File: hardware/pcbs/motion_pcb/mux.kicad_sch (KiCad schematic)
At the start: 2 parts, among them U3 74HC4051

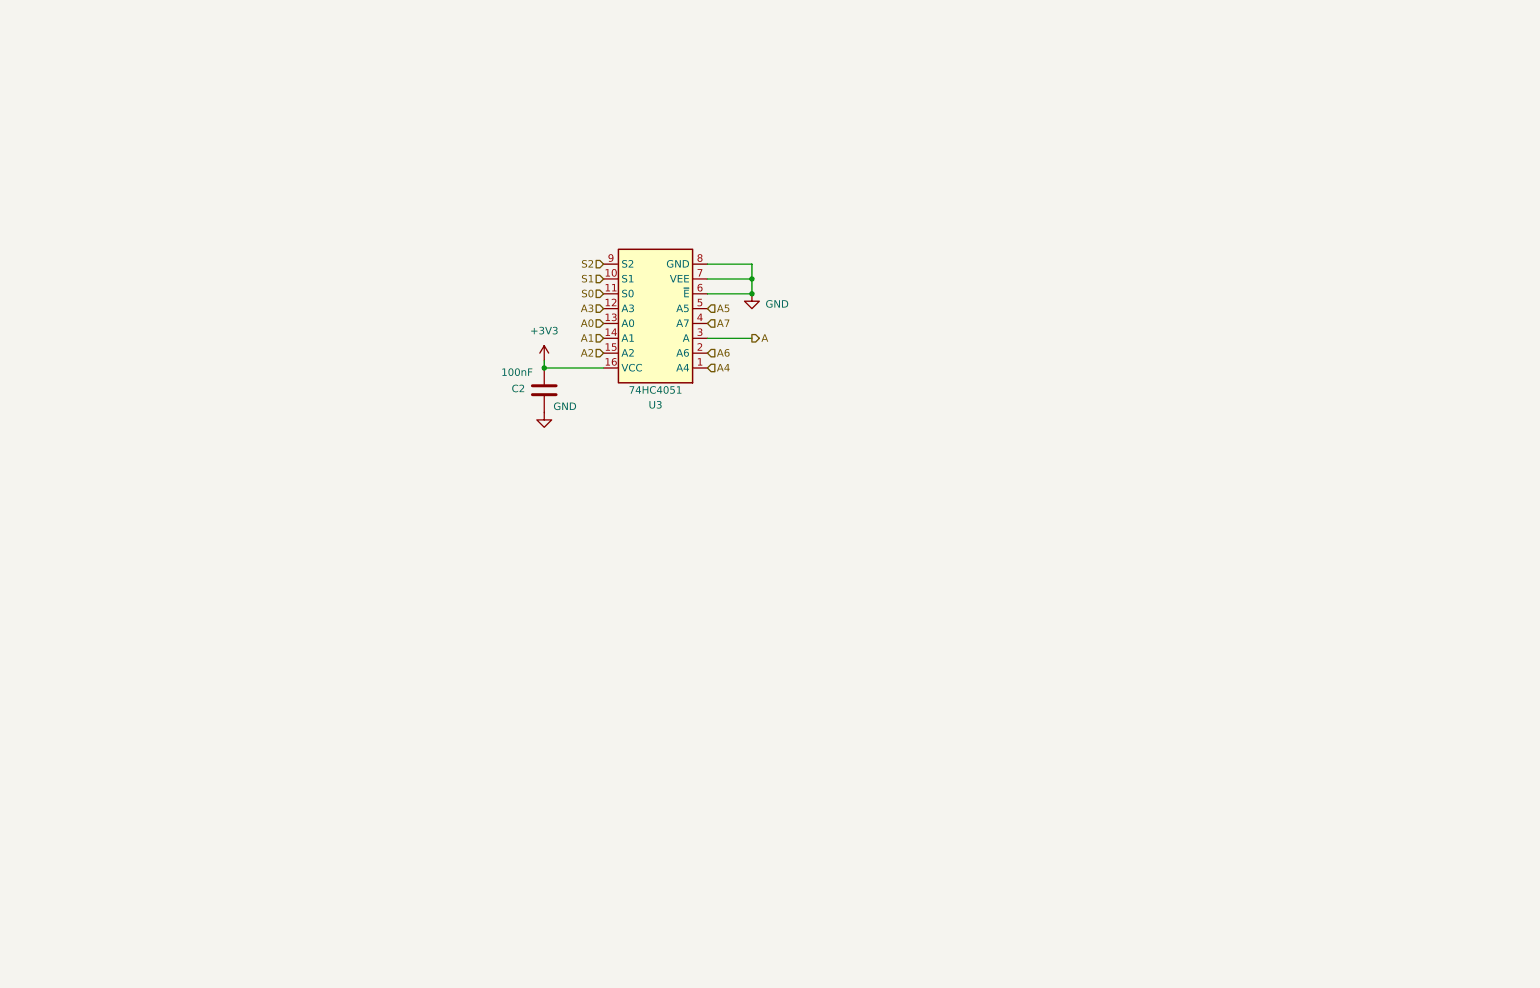
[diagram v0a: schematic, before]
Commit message: changing labels
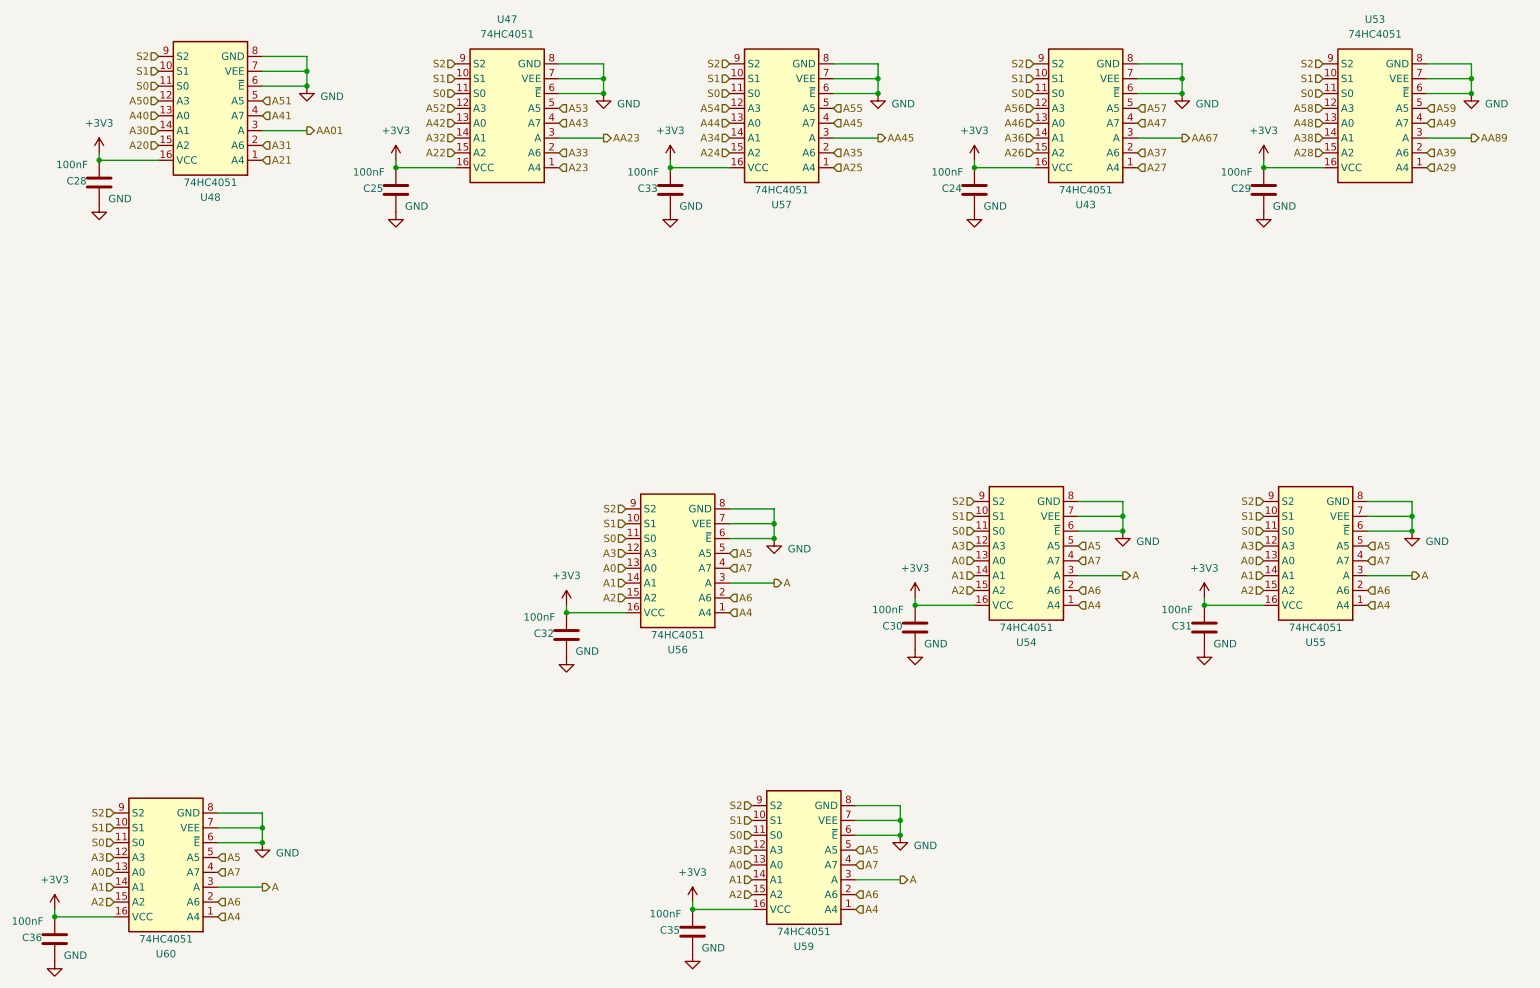
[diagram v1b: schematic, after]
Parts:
- added C24, C25, C28, C30, C31, C32, C33, C35, C36: 100nF, Capacitor_SMD:C_1206_3216Metric_Pad1.33x1.80mm_HandSolder, symbol Device:C
- added U43, U47, U48, U54, U55, U56, U57, U59, U60: 74HC4051, Package_SO:SOIC-16_3.9x9.9mm_P1.27mm, symbol 3dAudioSym:74HC4051
- U53: renamed from U3; footprint (none) -> Package_SO:SOIC-16_3.9x9.9mm_P1.27mm
- renumbered C2 to C29
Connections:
- net +3V3: now also C24.1, C25.1, C28.1, C30.1, C31.1, C32.1, C33.1, C35.1, C36.1, U43.16 (VCC), U47.16 (VCC), U48.16 (VCC), U54.16 (VCC), U55.16 (VCC), U56.16 (VCC), U57.16 (VCC), U59.16 (VCC), U60.16 (VCC)
- net A: now also U54.3 (A), U55.3 (A), U56.3 (A), U59.3 (A), U60.3 (A); no longer U53.3 (A)
- net A0: now also U54.13 (A0), U55.13 (A0), U56.13 (A0), U59.13 (A0), U60.13 (A0); no longer U53.13 (A0)
- net A1: now also U54.14 (A1), U55.14 (A1), U56.14 (A1), U59.14 (A1), U60.14 (A1); no longer U53.14 (A1)
- net A2: now also U54.15 (A2), U55.15 (A2), U56.15 (A2), U59.15 (A2), U60.15 (A2); no longer U53.15 (A2)
- net A3: now also U54.12 (A3), U55.12 (A3), U56.12 (A3), U59.12 (A3), U60.12 (A3); no longer U53.12 (A3)
- net A4: now also U54.1 (A4), U55.1 (A4), U56.1 (A4), U59.1 (A4), U60.1 (A4); no longer U53.1 (A4)
- net A5: now also U54.5 (A5), U55.5 (A5), U56.5 (A5), U59.5 (A5), U60.5 (A5); no longer U53.5 (A5)
- net A6: now also U54.2 (A6), U55.2 (A6), U56.2 (A6), U59.2 (A6), U60.2 (A6); no longer U53.2 (A6)
- net A7: now also U54.4 (A7), U55.4 (A7), U56.4 (A7), U59.4 (A7), U60.4 (A7); no longer U53.4 (A7)
- net GND: now also C24.2, C25.2, C28.2, C30.2, C31.2, C32.2, C33.2, C35.2, C36.2, U43.6 (~{E}), U43.7 (VEE), U43.8 (GND), U47.6 (~{E}), U47.7 (VEE), U47.8 (GND), U48.6 (~{E}), U48.7 (VEE), U48.8 (GND), U54.6 (~{E}), U54.7 (VEE), U54.8 (GND), U55.6 (~{E}), U55.7 (VEE), U55.8 (GND), U56.6 (~{E}), U56.7 (VEE), U56.8 (GND), U57.6 (~{E}), U57.7 (VEE), U57.8 (GND), U59.6 (~{E}), U59.7 (VEE), U59.8 (GND), U60.6 (~{E}), U60.7 (VEE), U60.8 (GND)
- net S0: now also U43.11 (S0), U47.11 (S0), U48.11 (S0), U54.11 (S0), U55.11 (S0), U56.11 (S0), U57.11 (S0), U59.11 (S0), U60.11 (S0)
- net S1: now also U43.10 (S1), U47.10 (S1), U48.10 (S1), U54.10 (S1), U55.10 (S1), U56.10 (S1), U57.10 (S1), U59.10 (S1), U60.10 (S1)
- net S2: now also U43.9 (S2), U47.9 (S2), U48.9 (S2), U54.9 (S2), U55.9 (S2), U56.9 (S2), U57.9 (S2), U59.9 (S2), U60.9 (S2)
- new net A20: U48.15 (A2)
- new net A21: U48.1 (A4)
- new net A22: U47.15 (A2)
- new net A23: U47.1 (A4)
- new net A24: U57.15 (A2)
- new net A25: U57.1 (A4)
- new net A26: U43.15 (A2)
- new net A27: U43.1 (A4)
- new net A28: U53.15 (A2)
- new net A29: U53.1 (A4)
- new net A30: U48.14 (A1)
- new net A31: U48.2 (A6)
- new net A32: U47.14 (A1)
- new net A33: U47.2 (A6)
- new net A34: U57.14 (A1)
- new net A35: U57.2 (A6)
- new net A36: U43.14 (A1)
- new net A37: U43.2 (A6)
- new net A38: U53.14 (A1)
- new net A39: U53.2 (A6)
- new net A40: U48.13 (A0)
- new net A41: U48.4 (A7)
- new net A42: U47.13 (A0)
- new net A43: U47.4 (A7)
- new net A44: U57.13 (A0)
- new net A45: U57.4 (A7)
- new net A46: U43.13 (A0)
- new net A47: U43.4 (A7)
- new net A48: U53.13 (A0)
- new net A49: U53.4 (A7)
- new net A50: U48.12 (A3)
- new net A51: U48.5 (A5)
- new net A52: U47.12 (A3)
- new net A53: U47.5 (A5)
- new net A54: U57.12 (A3)
- new net A55: U57.5 (A5)
- new net A56: U43.12 (A3)
- new net A57: U43.5 (A5)
- new net A58: U53.12 (A3)
- new net A59: U53.5 (A5)
- new net AA01: U48.3 (A)
- new net AA23: U47.3 (A)
- new net AA45: U57.3 (A)
- new net AA67: U43.3 (A)
- new net AA89: U53.3 (A)
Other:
- moved on the sheet: C29, U53

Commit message: finished pcb motion.
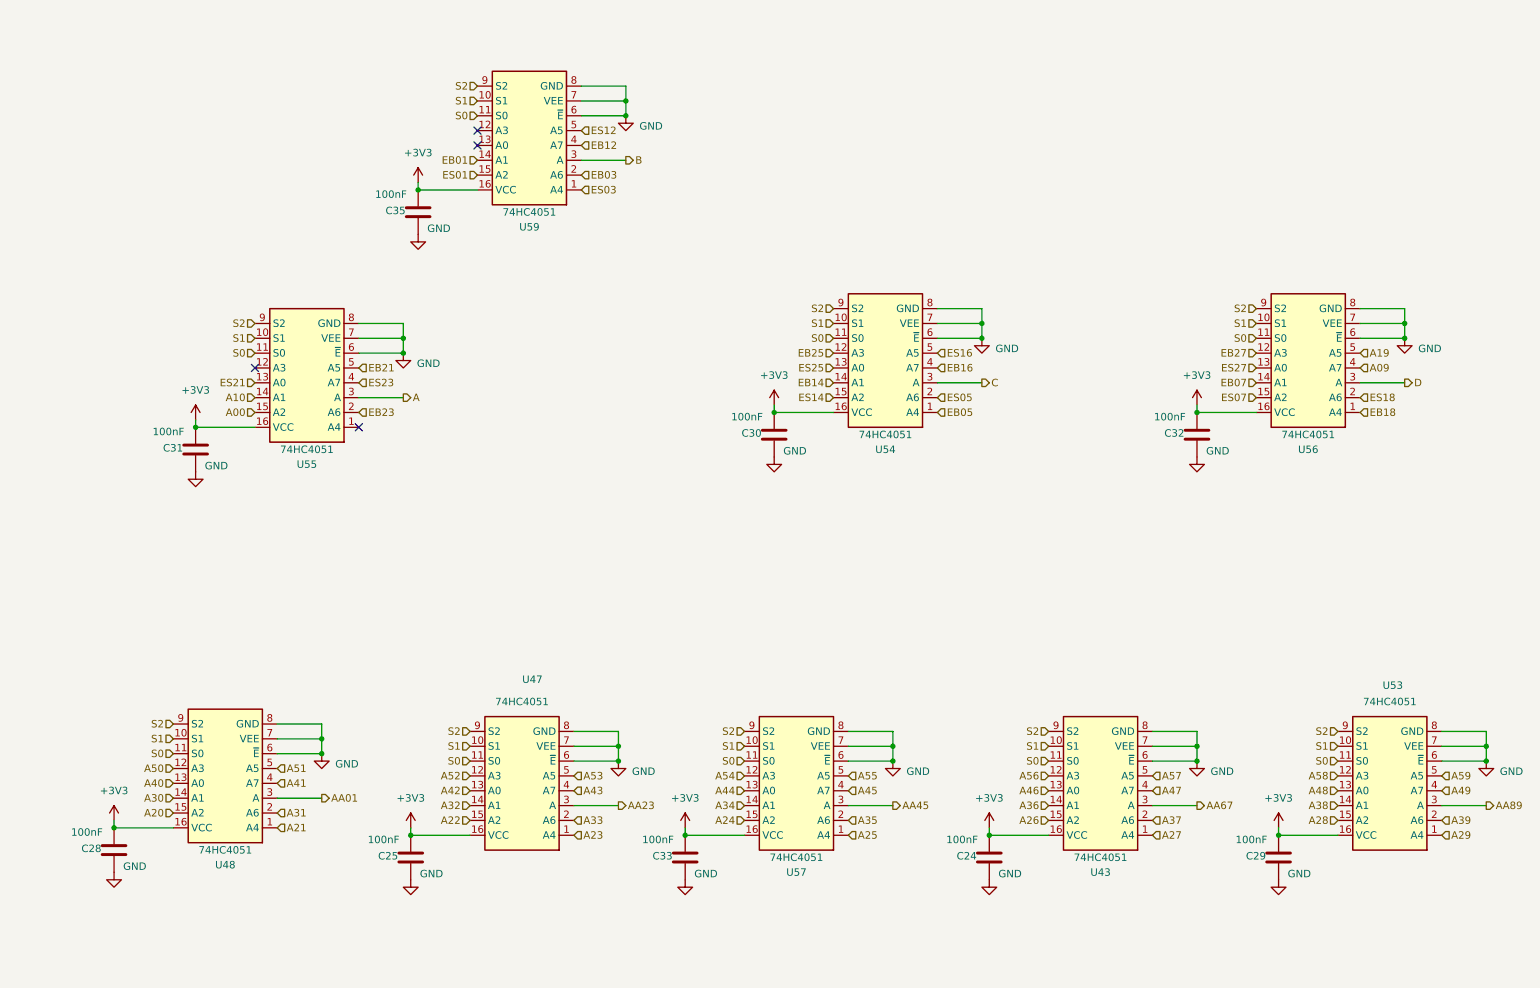
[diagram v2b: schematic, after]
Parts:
- removed C36: 100nF, Capacitor_SMD:C_1206_3216Metric_Pad1.33x1.80mm_HandSolder, symbol Device:C
- removed U60: 74HC4051, Package_SO:SOIC-16_3.9x9.9mm_P1.27mm, symbol 3dAudioSym:74HC4051
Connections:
- net A: no longer U54.3 (A), U56.3 (A), U59.3 (A)
- removed net A0: U54.13 (A0), U55.13 (A0), U56.13 (A0), U59.13 (A0)
- removed net A1: U54.14 (A1), U55.14 (A1), U56.14 (A1), U59.14 (A1)
- removed net A2: U54.15 (A2), U55.15 (A2), U56.15 (A2), U59.15 (A2)
- removed net A3: U54.12 (A3), U55.12 (A3), U56.12 (A3), U59.12 (A3)
- removed net A4: U54.1 (A4), U55.1 (A4), U56.1 (A4), U59.1 (A4)
- removed net A5: U54.5 (A5), U55.5 (A5), U56.5 (A5), U59.5 (A5)
- removed net A6: U54.2 (A6), U55.2 (A6), U56.2 (A6), U59.2 (A6)
- removed net A7: U54.4 (A7), U55.4 (A7), U56.4 (A7), U59.4 (A7)
- new net A00: U55.15 (A2)
- new net A09: U56.4 (A7)
- new net A10: U55.14 (A1)
- new net A19: U56.5 (A5)
- new net B: U59.3 (A)
- new net C: U54.3 (A)
- new net D: U56.3 (A)
- new net EB01: U59.14 (A1)
- new net EB03: U59.2 (A6)
- new net EB05: U54.1 (A4)
- new net EB07: U56.14 (A1)
- new net EB12: U59.4 (A7)
- new net EB14: U54.14 (A1)
- new net EB16: U54.4 (A7)
- new net EB18: U56.1 (A4)
- new net EB21: U55.5 (A5)
- new net EB23: U55.2 (A6)
- new net EB25: U54.12 (A3)
- new net EB27: U56.12 (A3)
- new net ES01: U59.15 (A2)
- new net ES03: U59.1 (A4)
- new net ES05: U54.2 (A6)
- new net ES07: U56.15 (A2)
- new net ES12: U59.5 (A5)
- new net ES14: U54.15 (A2)
- new net ES16: U54.5 (A5)
- new net ES18: U56.2 (A6)
- new net ES21: U55.13 (A0)
- new net ES23: U55.4 (A7)
- new net ES25: U54.13 (A0)
- new net ES27: U56.13 (A0)
- no-connect marks 0 -> 4
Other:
- moved on the sheet: C24, C25, C28, C29, C30, C31, C32, C33, C35, U43, U47, U48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
